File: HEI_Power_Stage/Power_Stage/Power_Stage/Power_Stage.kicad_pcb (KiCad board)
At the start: 6 copper layers, 137.3 x 65 mm, 169 parts, among them IC1 ACS730KLCTR-65ABT, IC10 AHV85111KNHTR, IC11 AHV85111KNHTR, IC12 AMC3311QDWERQ1, IC2 ACS730KLCTR-65ABT, IC3 ACS730KLCTR-65ABT, IC5 AHV85111KNHTR, IC6 AHV85111KNHTR, IC7 AHV85111KNHTR, IC8 AHV85111KNHTR, IC9 ACS730KLCTR-65ABT, J1 Screw_Terminal_01x01, J2 Screw_Terminal_01x01, J3 Screw_Terminal_01x01, J4 Screw_Terminal_01x01, J5 Screw_Terminal_01x01, J8 Conn_02x07_Odd_Even, J9 Conn_02x07_Odd_Even, Q1 EPC2304ENGRT, Q2 EPC2304ENGRT, Q3 EPC2304ENGRT, Q4 EPC2304ENGRT, Q5 EPC2304ENGRT, Q6 EPC2304ENGRT

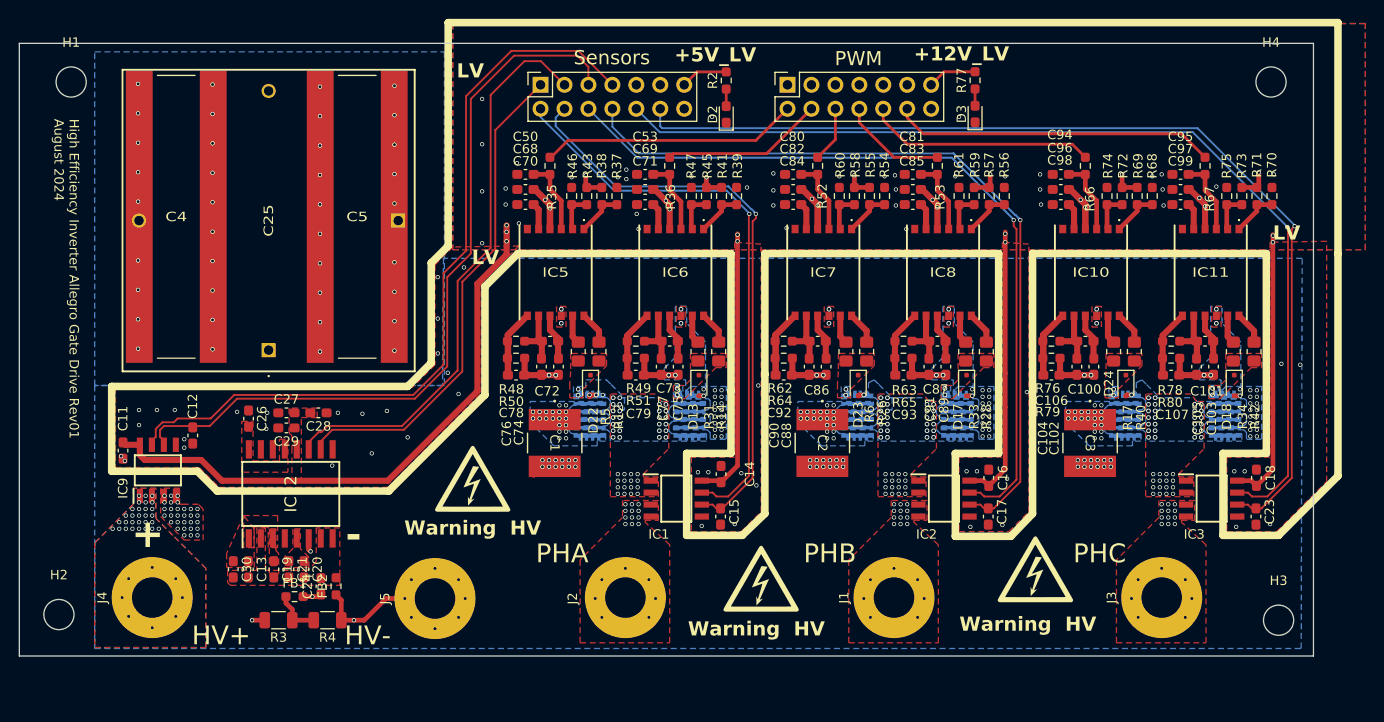
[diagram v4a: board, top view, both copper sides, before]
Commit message: changed dimensions and hole spacing
70x140mm
holes 4mm from edges on top left and right, 16mm from bottom
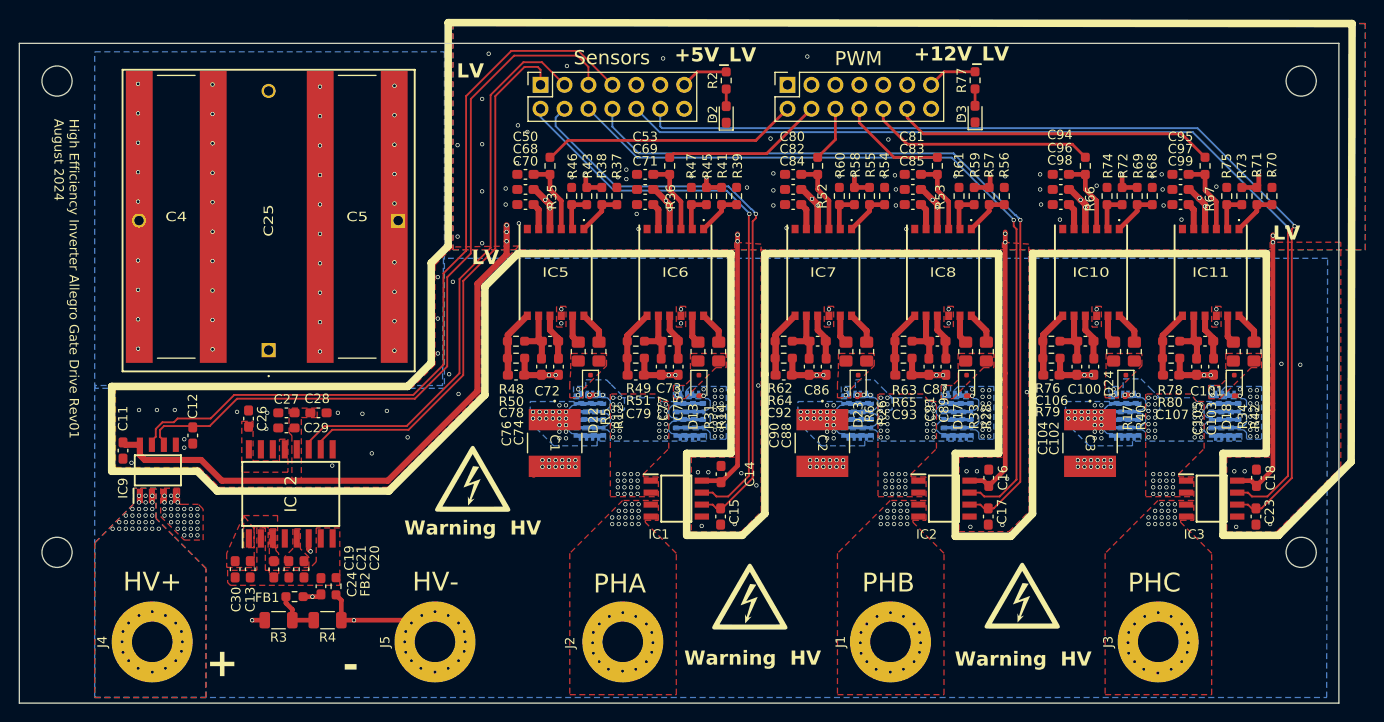
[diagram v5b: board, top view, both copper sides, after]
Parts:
- moved H3 7.59 mm to (233.0, 95.1)
- moved H2 6.60 mm to (101.0, 95.1)
- moved J1 4.71 mm to (189.4, 104.6)
- moved J3 4.71 mm to (217.8, 104.6)
- moved J2 4.71 mm to (161.0, 104.6)
- moved J4 4.70 mm to (111.1, 104.6)
- moved J5 4.60 mm to (141.1, 104.6)
- moved H4 3.20 mm to (233.0, 45.1)
- moved G*** 3.13 mm to (203.4, 99.7)
- moved G*** 2.25 mm to (174.5, 99.8)
- moved H1 1.50 mm to (101.0, 45.1)
- moved C13 0.20 mm to (121.5, 96.9)
- moved C30 0.20 mm to (119.9, 96.9)
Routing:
- net /DCV_{sense}-: track 52.8 -> 57.7 mm
- net /Phase3/SW: track 6.12 -> 6.52 mm, vias 47 -> 49
- net /Phase2/SW: track 6.12 -> 6.52 mm, vias 47 -> 49
- net HV-: track 30.9 -> 30.8 mm, vias 130 -> 138
- net HV+in: vias 37 -> 45
- net GND: vias 81 -> 92
- net /PHC: vias 19 -> 33
- net /PHB: vias 19 -> 33
- net /PHA: vias 19 -> 33
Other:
- board size 137.3 x 65 mm -> 140 x 70 mm
